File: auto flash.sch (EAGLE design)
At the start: 8 parts, among them T1 s8050, T2 s8050

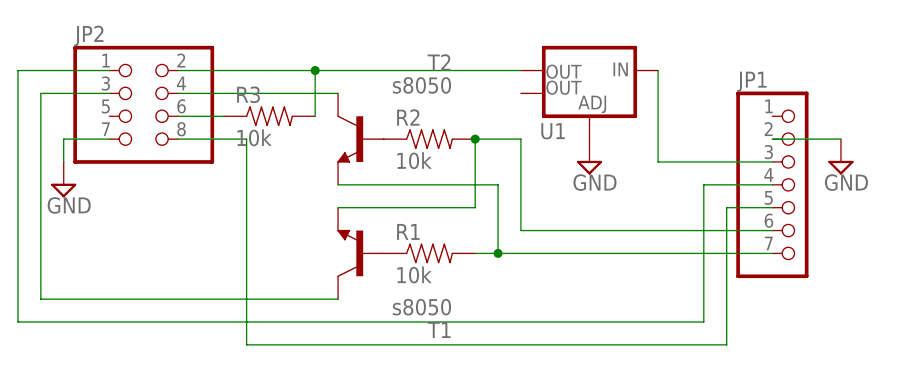
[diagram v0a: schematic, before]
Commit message: add esp-12, esp-07 adapter
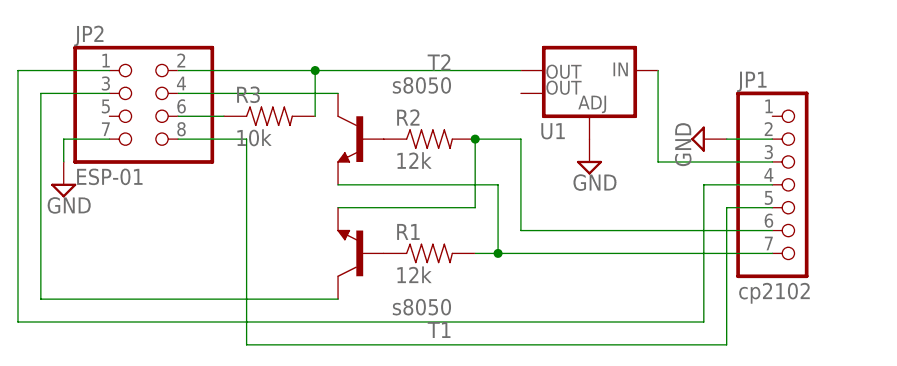
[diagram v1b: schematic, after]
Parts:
- JP1: value (none) -> cp2102
- JP2: value (none) -> ESP-01
- R1, R2: value 10k -> 12k
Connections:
- net N$10 renamed ESP-01
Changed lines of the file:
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@@
 <attribute name="OC_NEWARK" value="unknown"/>
 </part>
-<part name="JP1" library="pinhead" deviceset="PINHD-1X7" device="/90"/>
-<part name="JP2" library="pinhead" deviceset="PINHD-2X4" device=""/>
+<part name="JP1" library="pinhead" deviceset="PINHD-1X7" device="/90" value="cp2102"/>
+<part name="JP2" library="pinhead" deviceset="PINHD-2X4" device="" value="ESP-01"/>
 <part name="U1" library="SparkFun-PowerIC" deviceset="V_REG_LM1117" device="SOT223"/>
 <part name="SUPPLY1" library="supply2" deviceset="GND" device=""/>
@@
 <part name="SUPPLY3" library="supply2" deviceset="GND" device=""/>
 <part name="R3" library="SparkFun-Resistors" deviceset="0.3OHM-1/8W-1%(0805)" device="" value="10k"/>
-<part name="R1" library="SparkFun-Resistors" deviceset="0.3OHM-1/8W-1%(0805)" device="" value="10k"/>
-<part name="R2" library="SparkFun-Resistors" deviceset="0.3OHM-1/8W-1%(0805)" device="" value="10k"/>
+<part name="R1" library="SparkFun-Resistors" deviceset="0.3OHM-1/8W-1%(0805)" device="" value="12k"/>
+<part name="R2" library="SparkFun-Resistors" deviceset="0.3OHM-1/8W-1%(0805)" device="" value="12k"/>
 </parts>
 <sheets>
@@
 <instance part="SUPPLY1" gate="GND" x="78.74" y="45.72"/>
 <instance part="SUPPLY2" gate="GND" x="20.32" y="43.18"/>
-<instance part="SUPPLY3" gate="GND" x="106.68" y="45.72"/>
+<instance part="SUPPLY3" gate="GND" x="91.44" y="48.26" rot="R270"/>
 <instance part="R3" gate="G$1" x="43.18" y="50.8"/>
 <instance part="R1" gate="G$1" x="60.96" y="35.56"/>
@@
 <pinref part="JP1" gate="A" pin="2"/>
 <pinref part="SUPPLY3" gate="GND" pin="GND"/>
-<wire x1="99.06" y1="48.26" x2="106.68" y2="48.26" width="0.1524" layer="91"/>
+<wire x1="99.06" y1="48.26" x2="93.98" y2="48.26" width="0.1524" layer="91"/>
 </segment>
 </net>
@@
 </segment>
 </net>
-<net name="N$10" class="0">
+<net name="ESP-01" class="0">
 <segment>
 <pinref part="JP1" gate="A" pin="4"/>
